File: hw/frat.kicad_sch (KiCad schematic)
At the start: 0 parts

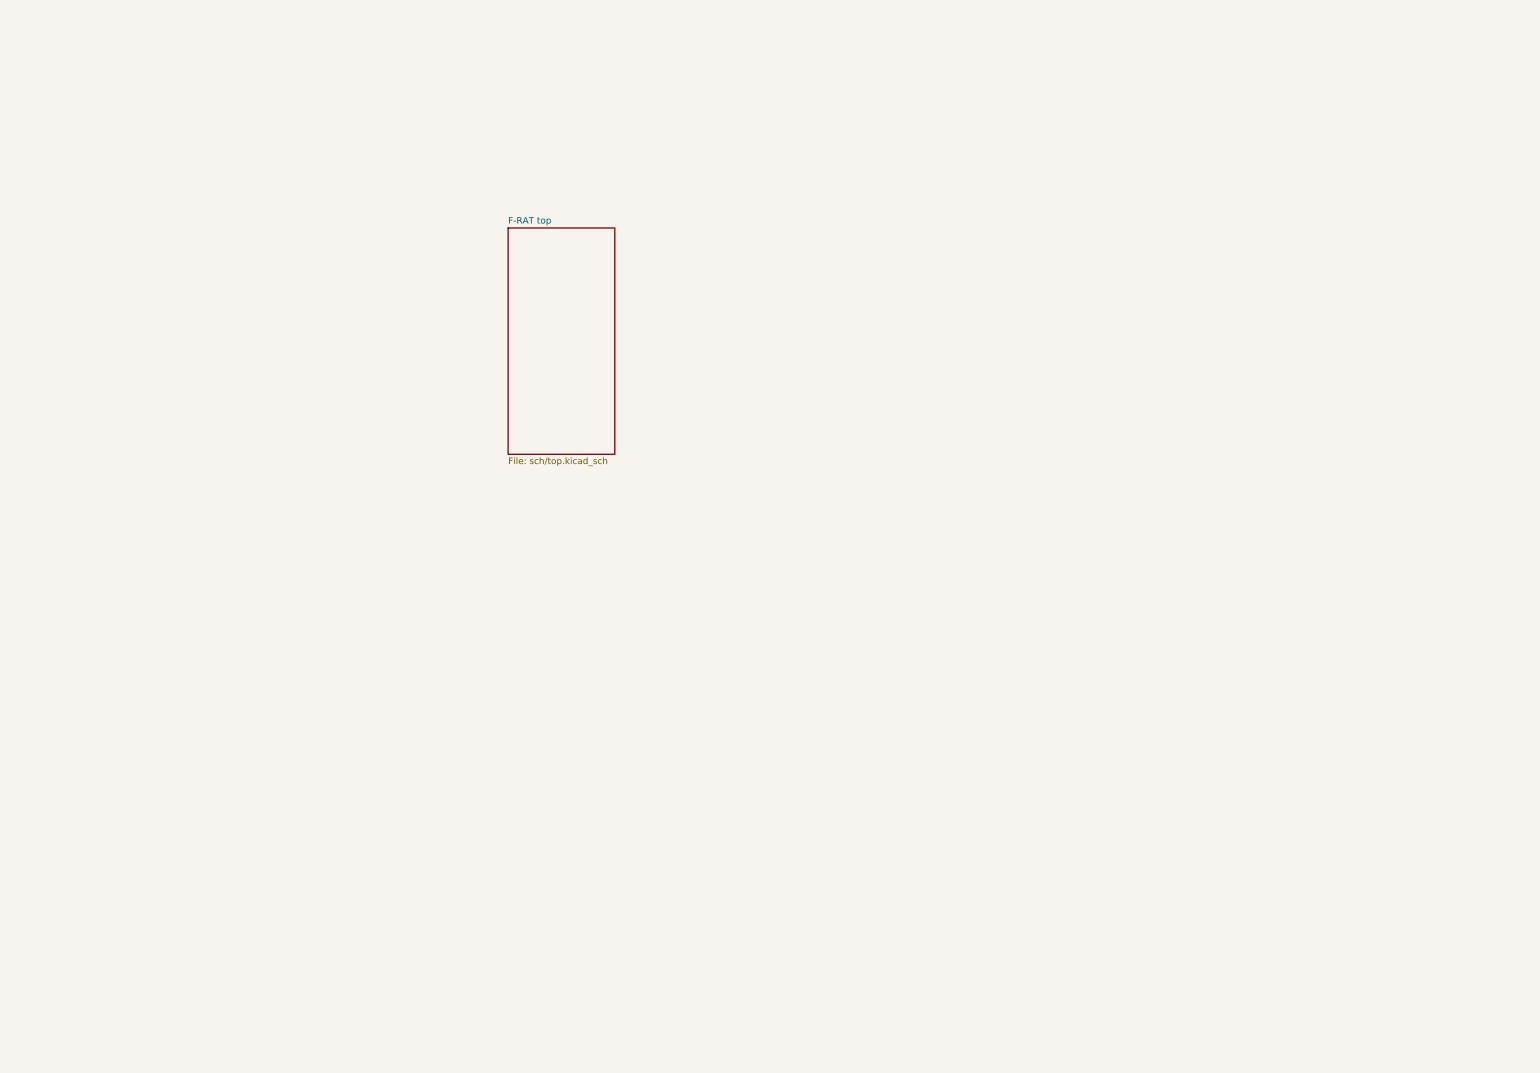
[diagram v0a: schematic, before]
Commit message: Fixed reference designators being wrong for hierarchical clones
Moving PCB and schematic files to separate folders caused reference designators to become cloned for right and left motor drivers, revert this change
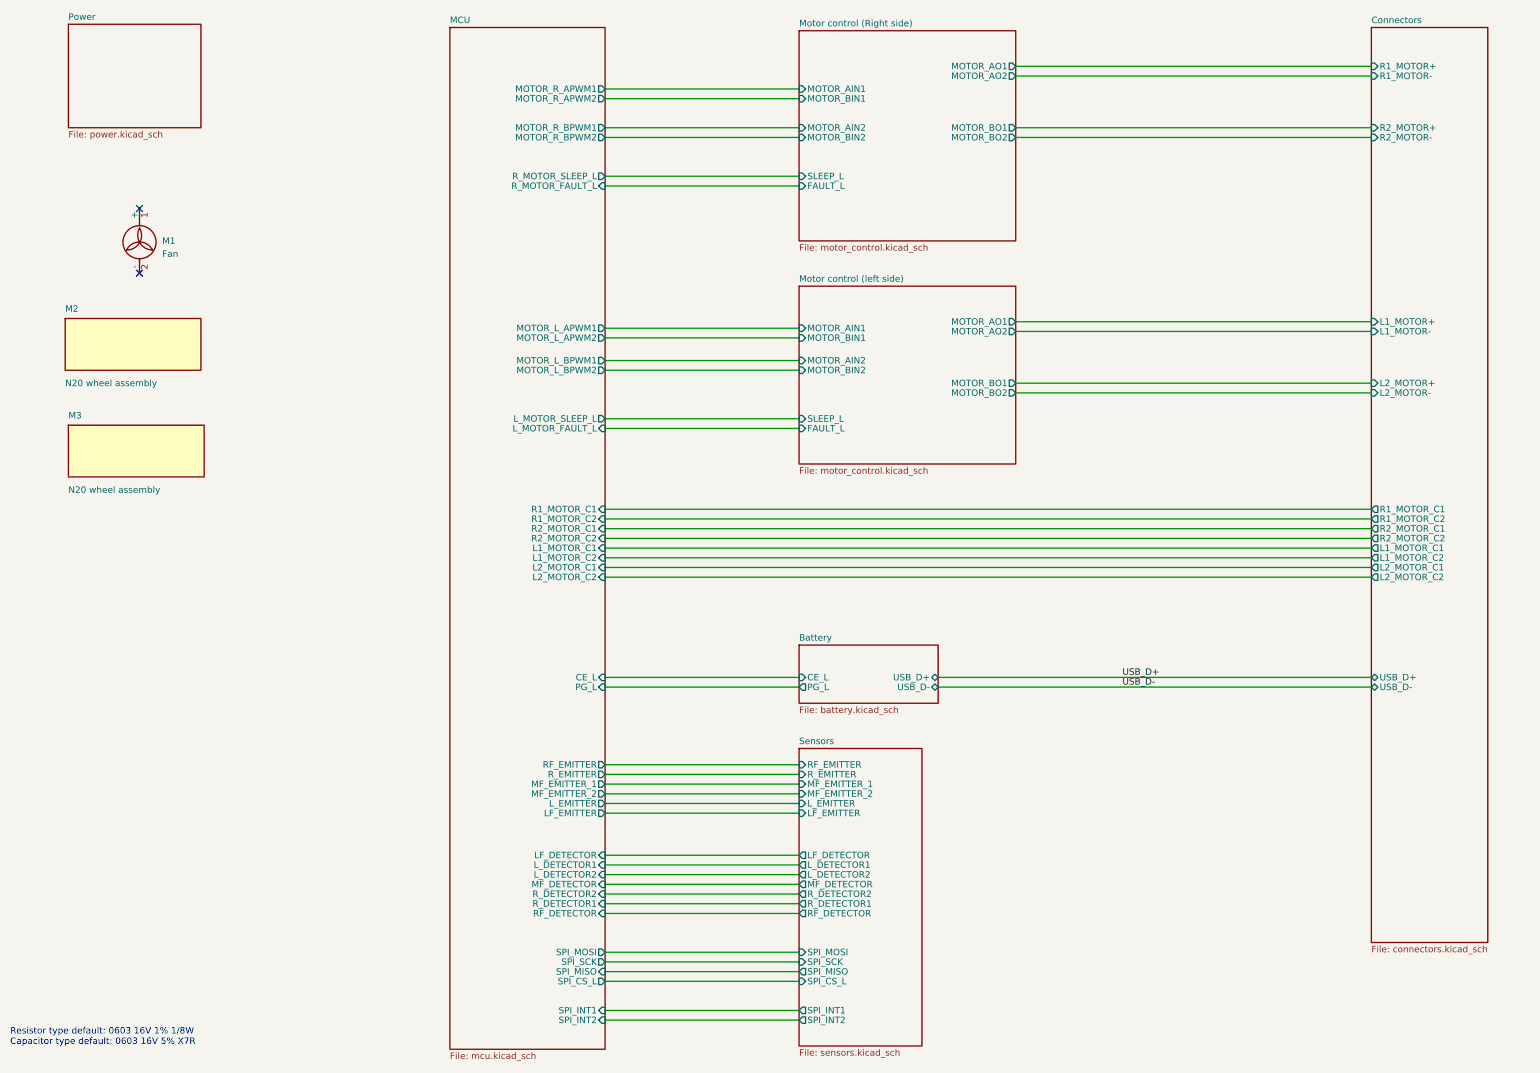
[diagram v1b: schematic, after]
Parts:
- added M1: Fan, lib:30mm fan, symbol Motor:Fan
- added M2, M3: N20 wheel assembly, lib:N20, symbol Assemblies:WHEEL_ASSEMBLY
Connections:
- no-connect marks 0 -> 2
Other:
- removed sheet F-RAT top
- added sheet Battery (battery.kicad_sch)
- added sheet Connectors (connectors.kicad_sch)
- added sheet MCU (mcu.kicad_sch)
- added sheet Motor control (Right side) (motor_control.kicad_sch)
- added sheet Motor control (left side) (motor_control.kicad_sch)
- added sheet Power (power.kicad_sch)
- added sheet Sensors (sensors.kicad_sch)
- note added: "Resistor type default: 0603 16V 1% 1/8W Capacitor type default: 0603 16V 5% X7R"
- company: (none) -> Data Respons R&D Services
- title: (none) -> F-RAT
